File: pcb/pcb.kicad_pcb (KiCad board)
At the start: 2 copper layers, 117 x 96.2 mm, 47 parts, among them J1 BATT, J2 BATT, SW1 SW_SPST, SW10 SW_SPST, SW11 SW_SPST, SW12 SW_SPST, SW13 SW_SPST, SW14 SW_SPST, SW15 SW_SPST, SW16 SW_SPST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

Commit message: fix: silkscreen
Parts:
- moved J2 4.12 mm to (187.0, 86.8)
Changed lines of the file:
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@@
   (net 36 "Net-(D18-A)")
   (footprint "scuffy:Battery" (layer "F.Cu")
-    (at 185.97 90.76 180)
+    (at 186.97 86.76 180)
     (descr "Molex PicoBlade Connector System, 53048-0210, 2 Pins per row (http://www.molex.com/pdm_docs/sd/530480210_sd.pdf), generated with kicad-footprint-generator")
     (tags "connector Molex PicoBlade top entry")
@@
         (effects (font (size 1 1) (thickness 0.15)))
     )
-    (fp_line (start -2.625 2.51) (end -1.355 2.51)
+    (fp_line (start -2.635 -2.5) (end -1.365 -2.5)
       (stroke (width 0.2) (type default)) (layer "B.SilkS"))
-    (fp_line (start -1.99 1.875) (end -1.99 3.145)
+    (fp_line (start -2 -3.135) (end -2 -1.865)
       (stroke (width 0.2) (type default)) (layer "B.SilkS"))
-    (fp_line (start 1.365 2.5) (end 2.635 2.5)
+    (fp_line (start 1.365 -2.5) (end 2.635 -2.5)
       (stroke (width 0.2) (type default)) (layer "B.SilkS"))
-    (fp_line (start -2.625 2.51) (end -1.355 2.51)
+    (fp_line (start -2.635 -2.5) (end -1.365 -2.5)
       (stroke (width 0.2) (type default)) (layer "F.SilkS"))
-    (fp_line (start -1.99 1.875) (end -1.99 3.145)
+    (fp_line (start -2 -3.135) (end -2 -1.865)
       (stroke (width 0.2) (type default)) (layer "F.SilkS"))
-    (fp_line (start 1.365 2.5) (end 2.635 2.5)
+    (fp_line (start 1.365 -2.5) (end 2.635 -2.5)
       (stroke (width 0.2) (type default)) (layer "F.SilkS"))
     (pad "1" thru_hole circle (at -2 0 180) (size 2 2) (drill 1) (layers "*.Cu" "*.Mask")
@@
     )
   )
-  (gr_line (start 141.392758 118.884559) (end 141.392758 120.375159)
-    (stroke (width 0.15) (type default)) (layer "Dwgs.User"))
-  (gr_line (start 169.892758 80.259559) (end 169.892758 82.259559)
-    (stroke (width 0.15) (type default)) (layer "Dwgs.User"))
-  (gr_line (start 112.892758 77.259559) (end 112.892758 79.259559)
-    (stroke (width 0.15) (type default)) (layer "Dwgs.User"))
-  (gr_line (start 131.892758 71.259559) (end 131.892758 73.259559)
-    (stroke (width 0.15) (type default)) (layer "Dwgs.User"))
-  (gr_line (start 150.892758 99.259559) (end 150.892758 100.750159)
-    (stroke (width 0.15) (type default)) (layer "Dwgs.User"))
-  (gr_line (start 131.892758 92.759559) (end 131.892758 94.250159)
-    (stroke (width 0.15) (type default)) (layer "Dwgs.User"))
-  (gr_line (start 112.892758 98.759559) (end 112.892758 100.250159)
-    (stroke (width 0.15) (type default)) (layer "Dwgs.User"))
-  (gr_line (start 93.892758 89.259559) (end 93.892758 91.259559)
-    (stroke (width 0.15) (type default)) (layer "Dwgs.User"))
-  (gr_line (start 112.892758 79.259559) (end 112.892758 81.276359)
-    (stroke (width 0.15) (type default)) (layer "Dwgs.User"))
-  (gr_line (start 150.892758 79.759559) (end 150.892758 81.776359)
-    (stroke (width 0.15) (type default)) (layer "Dwgs.User"))
-  (gr_line (start 150.892758 77.759559) (end 150.892758 79.759559)
-    (stroke (width 0.15) (type default)) (layer "Dwgs.User"))
-  (gr_line (start 131.892758 73.259559) (end 131.892758 75.276359)
-    (stroke (width 0.15) (type default)) (layer "Dwgs.User"))
-  (gr_line (start 169.892758 101.759559) (end 169.892758 103.250159)
-    (stroke (width 0.15) (type default)) (layer "Dwgs.User"))
-  (gr_line (start 93.892758 110.759559) (end 93.892758 112.250159)
-    (stroke (width 0.15) (type default)) (layer "Dwgs.User"))
-  (gr_line (start 169.892758 82.259559) (end 169.892758 84.276359)
-    (stroke (width 0.15) (type default)) (layer "Dwgs.User"))
-  (gr_line (start 93.892758 91.259559) (end 93.892758 93.276359)
-    (stroke (width 0.15) (type default)) (layer "Dwgs.User"))
   (gr_arc (start 102.892758 117.759559) (mid 103.0392 117.406) (end 103.392758 117.259559)
     (stroke (width 0.1) (type solid)) (layer "Edge.Cuts"))

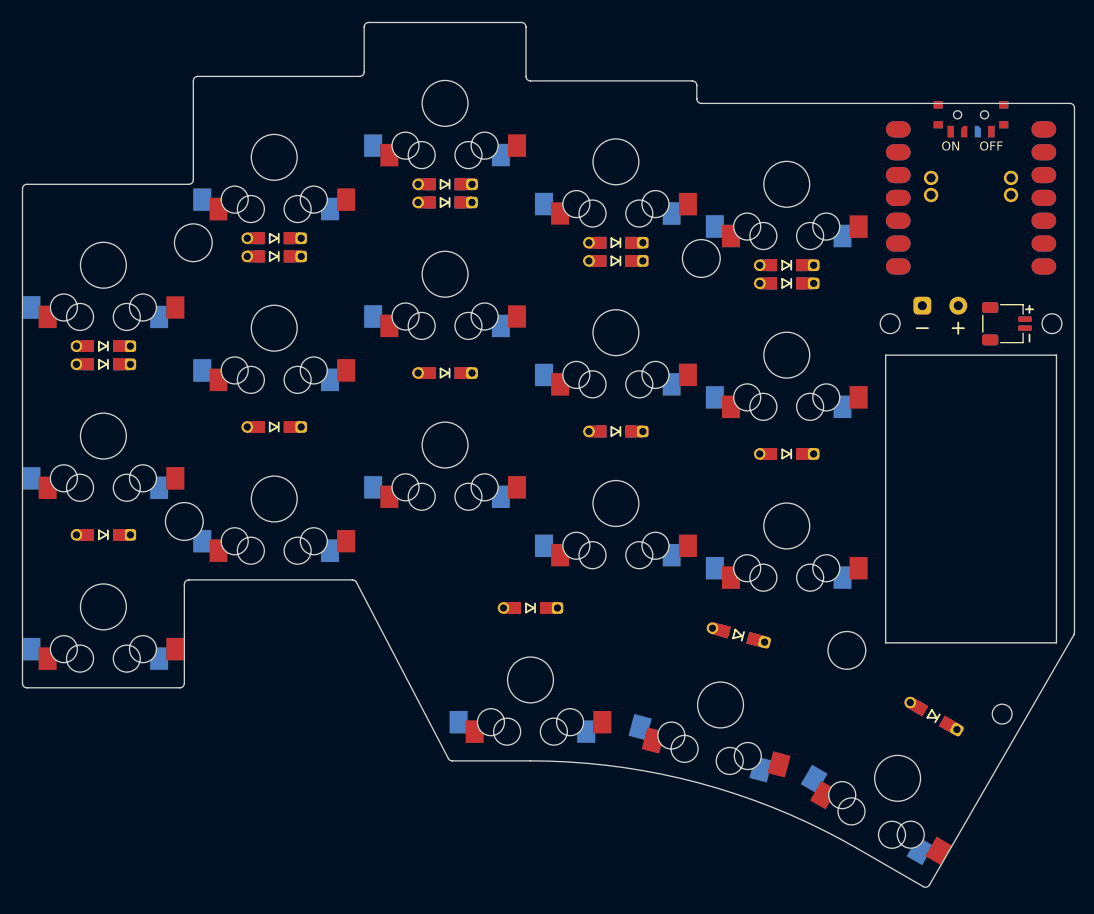
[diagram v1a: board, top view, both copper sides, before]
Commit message: fix: diode placement
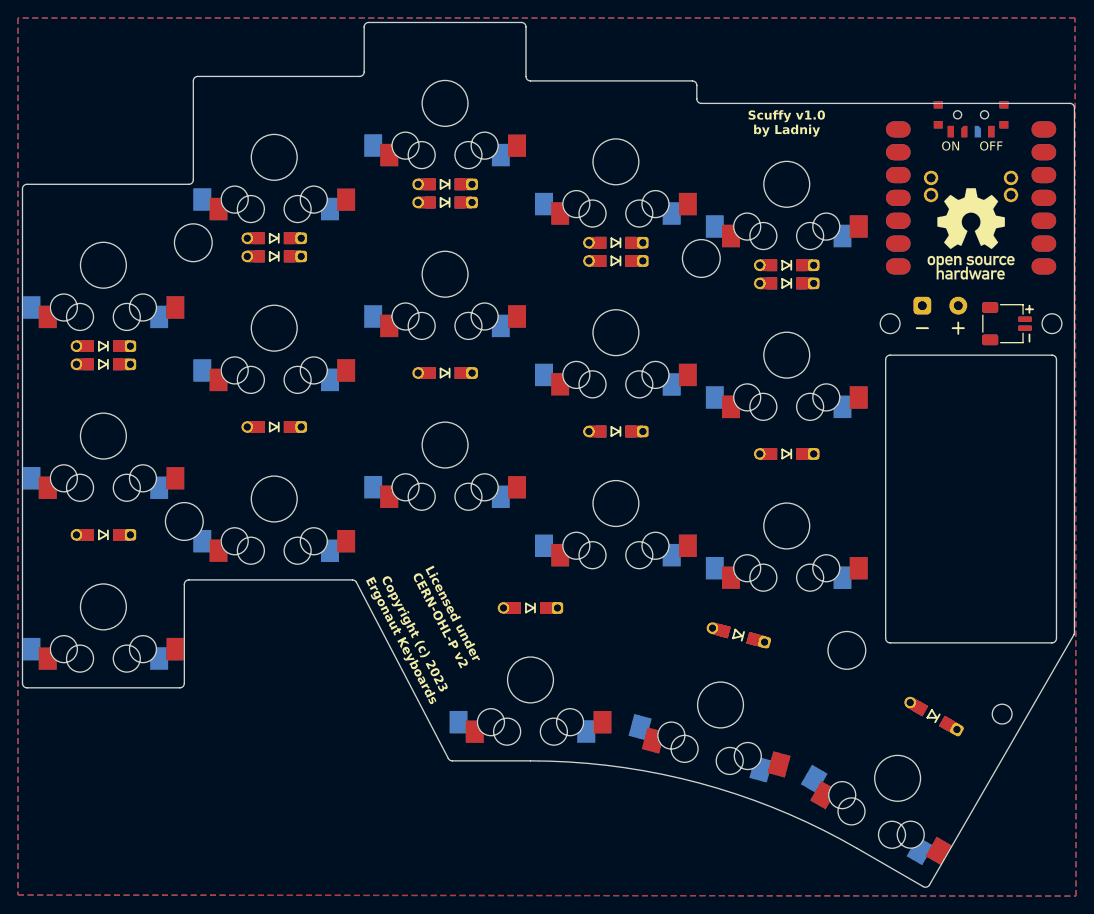
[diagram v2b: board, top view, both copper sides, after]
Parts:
- added G1: LOGO, scuffy:OSHW-logo, F.Cu at (190.4, 78.8)
- added G2: LOGO, scuffy:OSHW-logo, B.Cu at (190.4, 78.8)
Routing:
- added copper zone on B.Cu, net (none)
- added copper zone on F.Cu, net (none)
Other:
- outline, holes or cut-outs redrawn
- board text added: "Licensed under CERN-OHL-P v2 Copyright (c) 2023 Ergonaut Keyboards"
- board text added: "Scuffy v1.0 by Ladniy"

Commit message: feat: everything ready (no way)
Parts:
- PWR1: moved to B.Cu
- turned PWR1 to 180 degrees
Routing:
- net C0: track 0.00 -> 164.7 mm, vias 0 -> 6
- net C2: track 0.00 -> 155.8 mm, vias 0 -> 5
- net R2: track 0.00 -> 135.2 mm, vias 0 -> 1
- net C1: track 0.00 -> 134.2 mm, vias 0 -> 5
- net C3: track 0.00 -> 133.5 mm, vias 0 -> 5
- net R3: track 0.00 -> 123.3 mm, vias 0 -> 1
- net R0: track 0.00 -> 122.0 mm, vias 0 -> 1
- net C4: track 0.00 -> 118.9 mm, vias 0 -> 5
- net R1: track 0.00 -> 118.7 mm, vias 0 -> 1
- net B-: track 0.00 -> 57.7 mm, vias 0 -> 1
- net Net-(J1-Pin_1): track 0.00 -> 39.3 mm, vias 0 -> 1
- net Net-(D16-A): track 0.00 -> 19.6 mm, vias 0 -> 1
- net Net-(D6-A): track 0.00 -> 19.6 mm, vias 0 -> 1
- net Net-(D18-A): track 0.00 -> 19.6 mm, vias 0 -> 1
- net Net-(D14-A): track 0.00 -> 19.5 mm, vias 0 -> 1
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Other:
- board text added: "Copyright (c) 2023 Ergonaut Keyboards"
- board text added: "Ergonaut Scuffy v1.0 by Ladniy"
- board text added: "Licensed under CERN-OHL-P v2"
- board text removed: "Licensed under CERN-OHL-P v2 Copyright (c) 2023 Ergonaut Keyboards"
- board text removed: "Scuffy v1.0 by Ladniy"

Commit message: feat: a lot of things, more in future pr
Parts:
- added G***: LOGO, one:en_logo, F.Cu at (131.9, 115.8)
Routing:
- net R2: track 135.2 -> 145.8 mm, vias 1 -> 6
- net R0: track 122.0 -> 132.6 mm, vias 1 -> 6
- net R3: track 123.3 -> 133.3 mm, vias 1 -> 4
- net R1: track 118.7 -> 128.6 mm, vias 1 -> 6
- net Net-(D8-A): track 19.5 -> 22.4 mm, vias 1 -> 2
- net Net-(D7-A): track 19.5 -> 22.4 mm, vias 1 -> 2
- net Net-(D6-A): track 19.6 -> 22.6 mm, vias 1 -> 2
- net Net-(D13-A): track 19.5 -> 22.4 mm, vias 1 -> 2
- net Net-(D15-A): track 19.5 -> 22.4 mm, vias 1 -> 2
- net Net-(D14-A): track 19.5 -> 22.5 mm, vias 1 -> 2
- net Net-(D12-A): track 19.5 -> 22.4 mm, vias 1 -> 2
- net Net-(D11-A): track 19.5 -> 22.4 mm, vias 1 -> 2
- net Net-(D5-A): track 9.33 -> 12.3 mm, vias 1 -> 2
- net Net-(D4-A): track 9.17 -> 12.1 mm, vias 1 -> 2
- net Net-(D1-A): track 9.33 -> 12.3 mm, vias 1 -> 2
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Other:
- board size 117 x 96.2 mm -> 117 x 96 mm
- board text added: "Ergonaut One S v1.0 by Ladniy"
- board text removed: "Ergonaut Scuffy v1.0 by Ladniy"
